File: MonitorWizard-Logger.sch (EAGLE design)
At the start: 40 parts, among them CON1 MICROSD, IC1 LD117AV33, J1 22-27-2041-04, J2 22-27-2041-04, J3 22-27-2041-04, U1 DHT22, U2 RFM69HW, U3 LTC3531, U4-NRF24L01 NRF24L01+-PCB-AERIAL, U6 ATMEGA328P-PU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

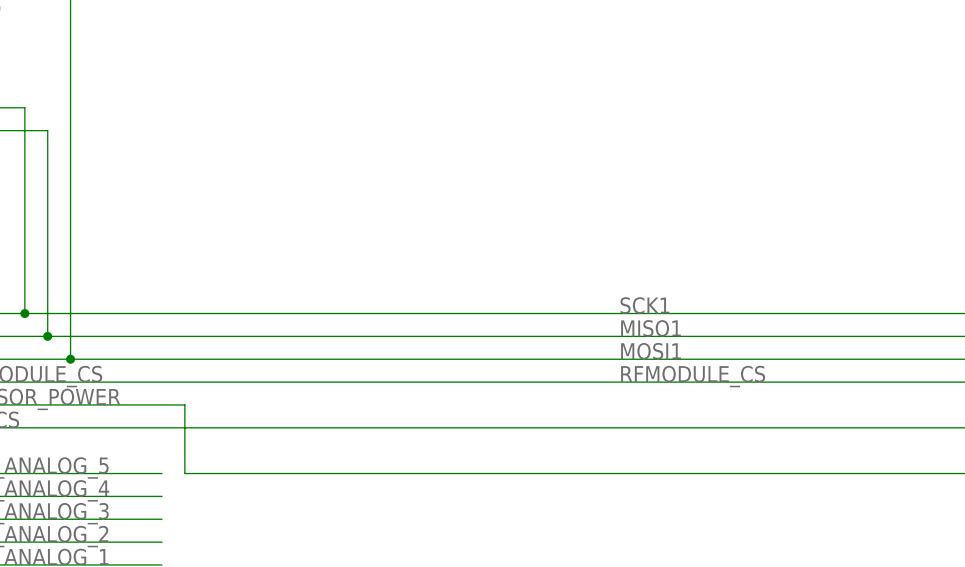
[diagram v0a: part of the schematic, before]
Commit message: Route remaining wires. Still needs the following: Confirm SD card current draw (idle, writing) - is a FET required to power the SD card down? Impedance matching SPI lines / SPI routing improvements? Full DRC check / capabilities of board house around power circuitry Any other improvements / errors before sending off?
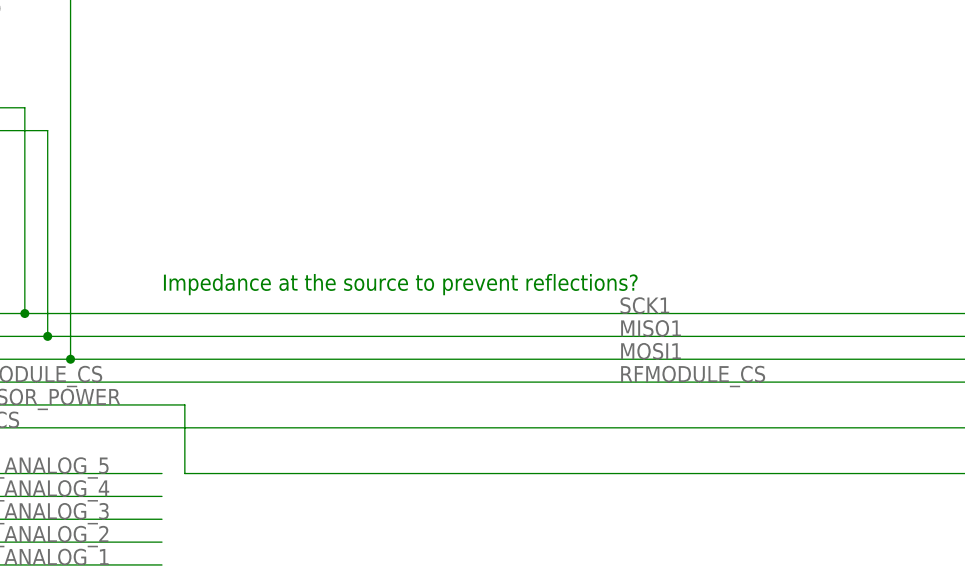
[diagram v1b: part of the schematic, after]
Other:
- note added: "Impedance at the source to prevent reflections?"
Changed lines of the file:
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@@
 <text x="393.7" y="-309.88" size="1.778" layer="91">TODO use electrolytic somewhere nearby</text>
 <text x="167.64" y="-88.9" size="1.778" layer="91">5V (not used)</text>
+<text x="193.04" y="-129.54" size="1.778" layer="91">Impedance at the source to prevent reflections?</text>
 </plain>
 <instances>

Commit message: More silkscreen fixes, move power jack to make more room for screw, tweak spacing of sensor connectors.
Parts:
- renumbered RF_CURRENT to I_RF, SENSOR_CURRENT to I_SENSE
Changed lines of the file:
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@@
 <part name="C13" library="rcl" deviceset="C-EU" device="025-024X044" value="0.1u"/>
 <part name="U4-NRF24L01" library="Radios" deviceset="NRF24L01+" device="-PCB-AERIAL"/>
-<part name="RF_CURRENT" library="Probes" deviceset="CURRENT_MEASURE" device="_0.4A"/>
+<part name="I_RF" library="Probes" deviceset="CURRENT_MEASURE" device="_0.4A"/>
 <part name="ICSP2" library="SmartPrj" deviceset="PINHD-2X3" device="" value="3x2 M"/>
 <part name="AER" library="solpad" deviceset="LSP10" device=""/>
@@
 <part name="X3" library="SmartPrj" deviceset="POWERSUPPLY_DC21MM" device="X"/>
 <part name="FD4" library="SmartPrj" deviceset="FIDUCIALMOUNT" device=""/>
-<part name="SENSOR_CURRENT" library="Probes" deviceset="CURRENT_MEASURE" device="_0.4A"/>
+<part name="I_SENSE" library="Probes" deviceset="CURRENT_MEASURE" device="_0.4A"/>
 <part name="U1" library="RHT03_DHT-22_AM2302" deviceset="RHT03_DHT-22_AM2302" device="" value="DHT22"/>
 <part name="R3" library="resistor" deviceset="R-EU_" device="0207/10" value="10K"/>
@@
 <instance part="C13" gate="G$1" x="101.6" y="-180.34" rot="R180"/>
 <instance part="U4-NRF24L01" gate="G$1" x="459.74" y="-109.22" rot="R180"/>
-<instance part="RF_CURRENT" gate="G$1" x="439.42" y="-330.2"/>
+<instance part="I_RF" gate="G$1" x="439.42" y="-330.2"/>
 <instance part="ICSP2" gate="A" x="160.02" y="-96.52"/>
 <instance part="AER" gate="1" x="408.94" y="-116.84" rot="R270"/>
@@
 </instance>
 <instance part="FD4" gate="G$1" x="599.44" y="-88.9"/>
-<instance part="SENSOR_CURRENT" gate="G$1" x="487.68" y="-330.2"/>
+<instance part="I_SENSE" gate="G$1" x="487.68" y="-330.2"/>
 <instance part="U1" gate="G$1" x="154.94" y="-365.76"/>
 <instance part="R3" gate="G$1" x="119.38" y="-355.6" rot="R90"/>
@@
 <wire x1="421.64" y1="-363.22" x2="439.42" y2="-363.22" width="0.1524" layer="91"/>
 <label x="419.1" y="-363.22" size="1.778" layer="95"/>
-<pinref part="RF_CURRENT" gate="G$1" pin="P$2"/>
+<pinref part="I_RF" gate="G$1" pin="P$2"/>
 <wire x1="439.42" y1="-337.82" x2="439.42" y2="-363.22" width="0.1524" layer="91"/>
 </segment>
@@
 <net name="3V3" class="0">
 <segment>
-<pinref part="RF_CURRENT" gate="G$1" pin="P$1"/>
+<pinref part="I_RF" gate="G$1" pin="P$1"/>
 <wire x1="439.42" y1="-322.58" x2="439.42" y2="-302.26" width="0.1524" layer="91"/>
 <label x="441.96" y="-312.42" size="1.778" layer="95"/>
@@
 <net name="SENSOR_POWER" class="0">
 <segment>
-<pinref part="SENSOR_CURRENT" gate="G$1" pin="P$1"/>
+<pinref part="I_SENSE" gate="G$1" pin="P$1"/>
 <wire x1="487.68" y1="-322.58" x2="487.68" y2="-149.86" width="0.1524" layer="91"/>
 <wire x1="487.68" y1="-149.86" x2="195.58" y2="-149.86" width="0.1524" layer="91"/>
@@
 <wire x1="462.28" y1="-363.22" x2="487.68" y2="-363.22" width="0.1524" layer="91"/>
 <label x="462.28" y="-363.22" size="1.778" layer="95"/>
-<pinref part="SENSOR_CURRENT" gate="G$1" pin="P$2"/>
+<pinref part="I_SENSE" gate="G$1" pin="P$2"/>
 <wire x1="487.68" y1="-363.22" x2="502.92" y2="-363.22" width="0.1524" layer="91"/>
 <wire x1="487.68" y1="-337.82" x2="487.68" y2="-363.22" width="0.1524" layer="91"/>

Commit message: Add electrolytic filter capacitor.
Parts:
- added C8: (no value), rcl:CPOL-EUE2.5-6
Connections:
- net 3V3: now also C8.+
- net GND: now also C8.-
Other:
- note removed: "TODO use electrolytic somewhere nearby"
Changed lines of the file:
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@@
 <part name="C6" library="rcl" deviceset="C-EU" device="025-024X044" value="0.1u"/>
 <part name="C7" library="rcl" deviceset="C-EU" device="025-024X044" value="0.1u"/>
+<part name="C8" library="rcl" deviceset="CPOL-EU" device="E2.5-6"/>
 </parts>
 <sheets>
@@
 <text x="449.58" y="-363.22" size="1.778" layer="91" rot="R90">RF module uses little current in low power mode - no need to disconnect</text>
 <text x="607.06" y="-177.8" size="1.778" layer="91">DAT1/DAT2 used for high speed comms only</text>
-<text x="393.7" y="-309.88" size="1.778" layer="91">TODO use electrolytic somewhere nearby</text>
 <text x="167.64" y="-88.9" size="1.778" layer="91">5V (not used)</text>
 <text x="193.04" y="-129.54" size="1.778" layer="91">Impedance at the source to prevent reflections?</text>
@@
 <instance part="C6" gate="G$1" x="695.96" y="-185.42" rot="R180"/>
 <instance part="C7" gate="G$1" x="381" y="-314.96" rot="R180"/>
+<instance part="C8" gate="G$1" x="391.16" y="-342.9"/>
 </instances>
 <busses>
@@
 <junction x="304.8" y="-383.54"/>
 <wire x1="355.6" y1="-393.7" x2="381" y2="-393.7" width="0.1524" layer="91"/>
-<wire x1="381" y1="-393.7" x2="520.7" y2="-393.7" width="0.1524" layer="91"/>
+<wire x1="381" y1="-393.7" x2="391.16" y2="-393.7" width="0.1524" layer="91"/>
+<wire x1="391.16" y1="-393.7" x2="520.7" y2="-393.7" width="0.1524" layer="91"/>
 <wire x1="520.7" y1="-393.7" x2="523.24" y2="-393.7" width="0.1524" layer="91"/>
 <wire x1="355.6" y1="-309.88" x2="355.6" y2="-393.7" width="0.1524" layer="91"/>
@@
 <wire x1="381" y1="-317.5" x2="381" y2="-393.7" width="0.1524" layer="91"/>
 <junction x="381" y="-393.7"/>
+<pinref part="C8" gate="G$1" pin="-"/>
+<wire x1="391.16" y1="-347.98" x2="391.16" y2="-393.7" width="0.1524" layer="91"/>
+<junction x="391.16" y="-393.7"/>
 </segment>
 <segment>
@@
 <pinref part="C7" gate="G$1" pin="2"/>
 <wire x1="381" y1="-309.88" x2="381" y2="-302.26" width="0.1524" layer="91"/>
-</segment>
-<segment>
+<wire x1="391.16" y1="-340.36" x2="391.16" y2="-302.26" width="0.1524" layer="91"/>
+<wire x1="391.16" y1="-302.26" x2="381" y2="-302.26" width="0.1524" layer="91"/>
+<junction x="381" y="-302.26"/>
+<pinref part="C8" gate="G$1" pin="+"/>
+</segment>
+<segment>

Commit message: Make the board smaller by pushing battery box to rear
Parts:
- removed VBAT: ALLIGATOR, Probes:ALLIGATOR
- U$2: device keystone:2464 -> keystone-nodrills:2464
- U3: device linear-sen:LTC3531 -> exported-lbrlinear-sen:LTC3531
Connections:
- net VBAT: no longer VBAT.BTM, VBAT.TOP
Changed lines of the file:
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@@
 <part name="AER" library="solpad" deviceset="LSP10" device=""/>
 <part name="GND" library="Probes" deviceset="ALLIGATOR" device=""/>
-<part name="VBAT" library="Probes" deviceset="ALLIGATOR" device=""/>
 <part name="X3" library="SmartPrj" deviceset="POWERSUPPLY_DC21MM" device="X"/>
 <part name="FD4" library="SmartPrj" deviceset="FIDUCIALMOUNT" device=""/>
@@
 <part name="R3" library="resistor" deviceset="R-EU_" device="0207/10" value="10K"/>
 <part name="U2" library="SparkFun-RF" deviceset="RFM69H" device="W"/>
-<part name="U3" library="linear-sen" deviceset="LTC3531" device=""/>
+<part name="U3" library="exported-lbrlinear-sen" deviceset="LTC3531" device=""/>
 <part name="L1" library="InductorsThru" deviceset="MURATA-1100R" device="" value="10uH"/>
 <part name="R1" library="resistor" deviceset="R-EU_" device="0207/10"/>
@@
 <part name="CON1" library="adafruit" deviceset="MICROSD" device=""/>
 <part name="U$1" library="adafruit" deviceset="SDMMC" device="06132"/>
-<part name="U$2" library="keystone" deviceset="2464" device=""/>
+<part name="U$2" library="keystone-nodrills" deviceset="2464" device=""/>
 <part name="J1" library="con-molex" deviceset="22-?-04" device="27-2041"/>
 <part name="J2" library="con-molex" deviceset="22-?-04" device="27-2041"/>
@@
 <instance part="AER" gate="1" x="408.94" y="-116.84" rot="R270"/>
 <instance part="GND" gate="G$1" x="525.78" y="-388.62" rot="R90"/>
-<instance part="VBAT" gate="G$1" x="525.78" y="-307.34" rot="R270"/>
 <instance part="X3" gate="G$1" x="309.88" y="-360.68" smashed="yes">
 <attribute name="NAME" x="299.72" y="-353.06" size="1.27" layer="94"/>
@@
 <net name="GND" class="2">
 <segment>
-<wire x1="528.32" y1="-393.7" x2="538.48" y2="-393.7" width="0.1524" layer="91"/>
+<wire x1="528.32" y1="-393.7" x2="541.02" y2="-393.7" width="0.1524" layer="91"/>
 <label x="406.4" y="-393.7" size="1.778" layer="95"/>
 <pinref part="GND" gate="G$1" pin="TOP"/>
-<wire x1="538.48" y1="-393.7" x2="541.02" y2="-393.7" width="0.1524" layer="91"/>
 <wire x1="523.24" y1="-393.7" x2="528.32" y2="-393.7" width="0.1524" layer="91"/>
 <junction x="523.24" y="-393.7"/>
@@
 <wire x1="586.74" y1="-327.66" x2="586.74" y2="-393.7" width="0.1524" layer="91"/>
 <wire x1="586.74" y1="-393.7" x2="551.18" y2="-393.7" width="0.1524" layer="91"/>
-<junction x="538.48" y="-393.7"/>
 <pinref part="R1" gate="G$1" pin="1"/>
-<wire x1="551.18" y1="-393.7" x2="538.48" y2="-393.7" width="0.1524" layer="91"/>
+<wire x1="551.18" y1="-393.7" x2="541.02" y2="-393.7" width="0.1524" layer="91"/>
 <wire x1="612.14" y1="-373.38" x2="612.14" y2="-393.7" width="0.1524" layer="91"/>
 <wire x1="612.14" y1="-393.7" x2="586.74" y2="-393.7" width="0.1524" layer="91"/>
@@
 <wire x1="421.64" y1="-363.22" x2="439.42" y2="-363.22" width="0.1524" layer="91"/>
 <label x="419.1" y="-363.22" size="1.778" layer="95"/>
+<wire x1="439.42" y1="-342.9" x2="439.42" y2="-363.22" width="0.1524" layer="91"/>
+<wire x1="436.88" y1="-342.9" x2="439.42" y2="-342.9" width="0.1524" layer="91"/>
 <pinref part="I_RF" gate="G$1" pin="P$2"/>
-<wire x1="439.42" y1="-337.82" x2="439.42" y2="-363.22" width="0.1524" layer="91"/>
+<wire x1="439.42" y1="-342.9" x2="439.42" y2="-337.82" width="0.1524" layer="91"/>
+<junction x="439.42" y="-342.9"/>
 </segment>
 </net>
@@
 <segment>
 <label x="523.24" y="-302.26" size="1.778" layer="95"/>
-<pinref part="VBAT" gate="G$1" pin="TOP"/>
-<wire x1="523.24" y1="-302.26" x2="528.32" y2="-302.26" width="0.1524" layer="91"/>
-<pinref part="VBAT" gate="G$1" pin="BTM"/>
 <pinref part="U3" gate="G$1" pin="VIN"/>
 <wire x1="574.04" y1="-309.88" x2="571.5" y2="-309.88" width="0.1524" layer="91"/>
@@
 <wire x1="551.18" y1="-309.88" x2="538.48" y2="-309.88" width="0.1524" layer="91"/>
 <wire x1="538.48" y1="-309.88" x2="538.48" y2="-302.26" width="0.1524" layer="91"/>
-<wire x1="538.48" y1="-302.26" x2="528.32" y2="-302.26" width="0.1524" layer="91"/>
-<junction x="528.32" y="-302.26"/>
+<wire x1="538.48" y1="-302.26" x2="520.7" y2="-302.26" width="0.1524" layer="91"/>
 <label x="558.8" y="-309.88" size="1.778" layer="95"/>
 <pinref part="U3" gate="G$1" pin="!SHDN"/>
@@
 <junction x="551.18" y="-309.88"/>
 <wire x1="520.7" y1="-345.44" x2="520.7" y2="-302.26" width="0.1524" layer="91"/>
-<wire x1="520.7" y1="-302.26" x2="523.24" y2="-302.26" width="0.1524" layer="91"/>
-<junction x="523.24" y="-302.26"/>
 <pinref part="U$2" gate="G$1" pin="+"/>
 </segment>
@@
 <net name="3V3" class="0">
 <segment>
+<label x="441.96" y="-312.42" size="1.778" layer="95"/>
+<wire x1="439.42" y1="-317.5" x2="439.42" y2="-302.26" width="0.1524" layer="91"/>
+<wire x1="439.42" y1="-317.5" x2="436.88" y2="-317.5" width="0.1524" layer="91"/>
 <pinref part="I_RF" gate="G$1" pin="P$1"/>
-<wire x1="439.42" y1="-322.58" x2="439.42" y2="-302.26" width="0.1524" layer="91"/>
-<label x="441.96" y="-312.42" size="1.778" layer="95"/>
-</segment>
-<segment>
+<wire x1="439.42" y1="-317.5" x2="439.42" y2="-322.58" width="0.1524" layer="91"/>
+<junction x="439.42" y="-317.5"/>
+</segment>
+<segment>
